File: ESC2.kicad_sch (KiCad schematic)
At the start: 35 parts, among them J10 MOTOR1, J9 SWD1, Q4 XRS306D, Q5 XRS306D, Q6 XRS306D, U10 STM32G071GBUxN, U11 DRV8300D

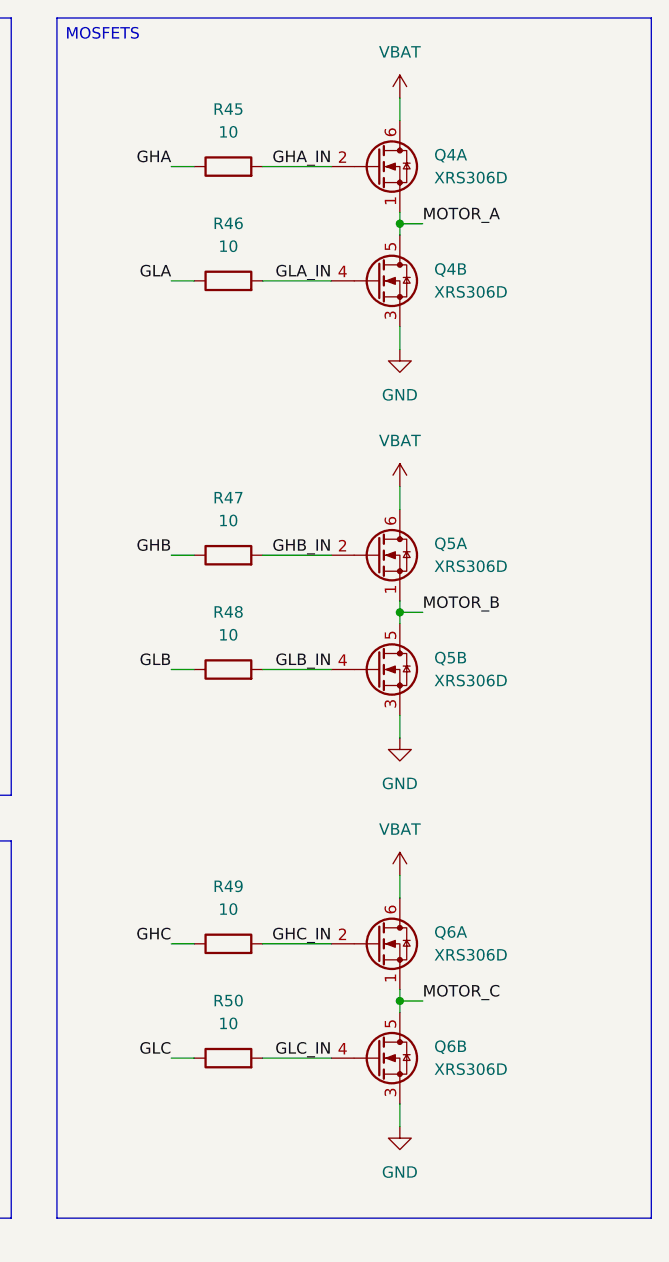
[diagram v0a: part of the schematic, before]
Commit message: License and ESC layout
Added a file extension to the license.
Updated the second ESC layout.

TODO:
Continue the ESC layout.
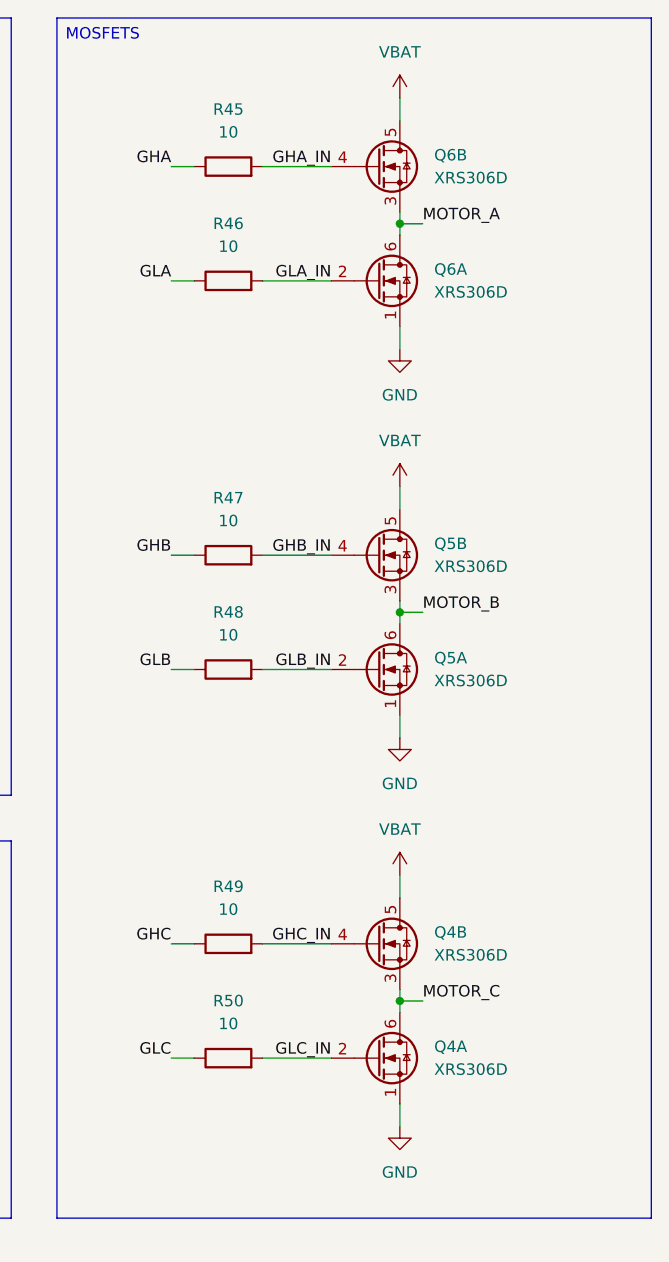
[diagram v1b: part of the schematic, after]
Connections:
- net GHA_IN: now also Q6.4 (G); no longer Q4.2 (G)
- net GHB_IN: now also Q5.4 (G); no longer Q5.2 (G)
- net GHC_IN: now also Q4.4 (G); no longer Q6.2 (G)
- net GLA_IN: now also Q6.2 (G); no longer Q4.4 (G)
- net GLB_IN: now also Q5.2 (G); no longer Q5.4 (G)
- net GLC_IN: now also Q4.2 (G); no longer Q6.4 (G)
- net GND: now also Q4.1 (S), Q5.1 (S), Q6.1 (S); no longer Q4.3 (S), Q5.3 (S), Q6.3 (S)
- net MOTOR_A: now also Q6.3 (S), Q6.6 (D); no longer Q4.1 (S), Q4.5 (D)
- net MOTOR_B: now also Q5.3 (S), Q5.6 (D); no longer Q5.1 (S), Q5.5 (D)
- net MOTOR_C: now also Q4.3 (S), Q4.6 (D); no longer Q6.1 (S), Q6.5 (D)
- net VBAT: now also Q4.5 (D), Q5.5 (D), Q6.5 (D); no longer Q4.6 (D), Q5.6 (D), Q6.6 (D)
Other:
- moved on the sheet: Q4A, Q4B, Q5A, Q5B, Q6A, Q6B

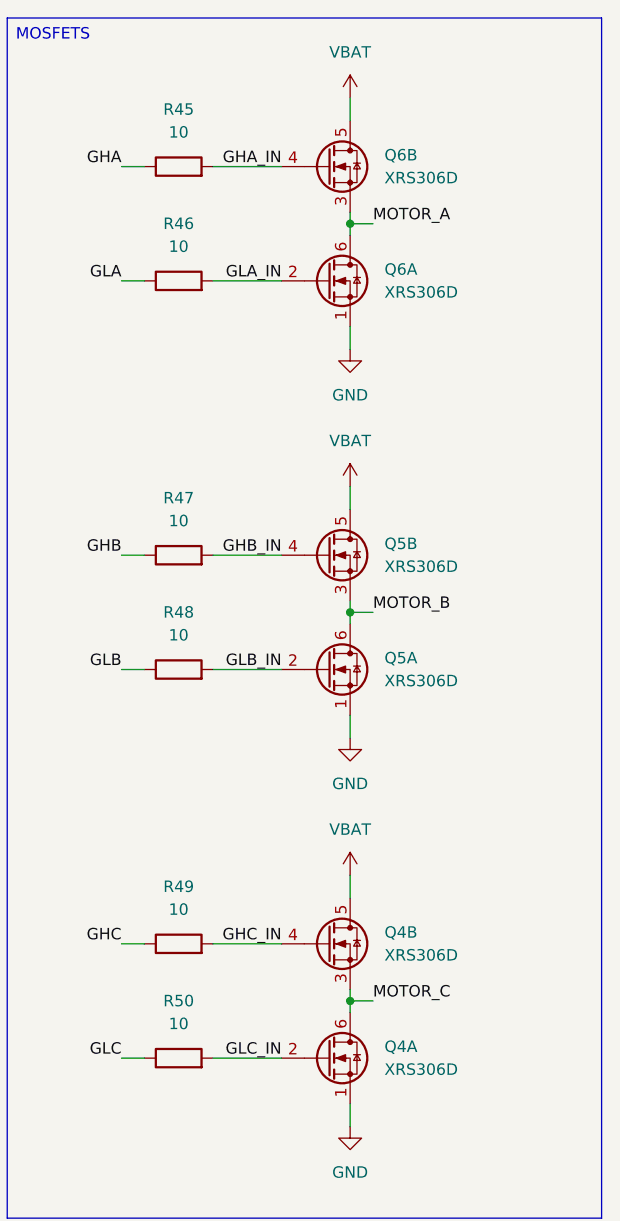
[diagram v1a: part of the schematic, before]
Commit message: MCU layout
Updated the schematic labels.
Continued the MCU layout.
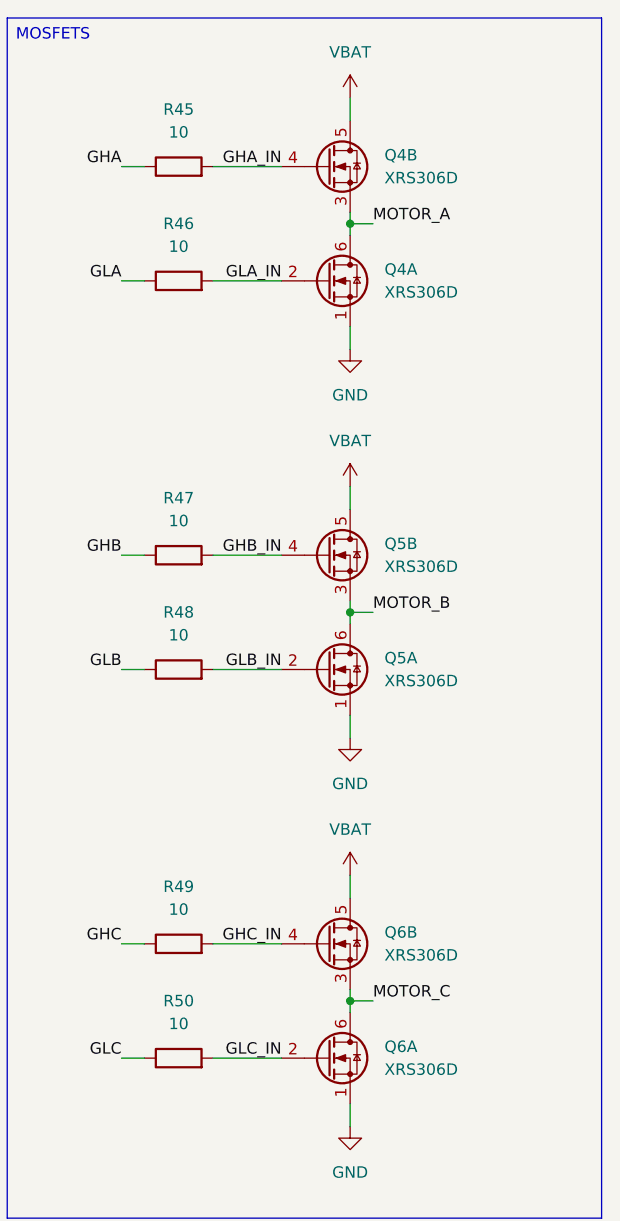
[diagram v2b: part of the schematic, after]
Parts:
- renumbered Q6 to Q4, Q4 to Q6
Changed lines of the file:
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@@
 		(dnp no)
 		(fields_autoplaced yes)
-		(property "Reference" "Q4"
+		(property "Reference" "Q6"
 			(at 250.19 124.4599 0)
 			(effects
@@
 			(project "ThunderHorse"
 				(path "/ac187c6c-fa53-41cc-bce1-6f39a42a92e8/807a5f6f-4255-4cf0-8d90-acd62bb18590/5c810e84-f116-497a-8ed3-5f68f4ce3b3e"
-					(reference "Q4")
+					(reference "Q6")
 					(unit 2)
 				)
@@
 		(dnp no)
 		(fields_autoplaced yes)
-		(property "Reference" "Q6"
+		(property "Reference" "Q4"
 			(at 250.19 38.0999 0)
 			(effects
@@
 			(project "ThunderHorse"
 				(path "/ac187c6c-fa53-41cc-bce1-6f39a42a92e8/807a5f6f-4255-4cf0-8d90-acd62bb18590/5c810e84-f116-497a-8ed3-5f68f4ce3b3e"
-					(reference "Q6")
+					(reference "Q4")
 					(unit 2)
 				)
@@
 		(dnp no)
 		(fields_autoplaced yes)
-		(property "Reference" "Q6"
+		(property "Reference" "Q4"
 			(at 250.19 50.7999 0)
 			(effects
@@
 			(project "ThunderHorse"
 				(path "/ac187c6c-fa53-41cc-bce1-6f39a42a92e8/807a5f6f-4255-4cf0-8d90-acd62bb18590/5c810e84-f116-497a-8ed3-5f68f4ce3b3e"
-					(reference "Q6")
+					(reference "Q4")
 					(unit 1)
 				)
@@
 		(dnp no)
 		(fields_autoplaced yes)
-		(property "Reference" "Q4"
+		(property "Reference" "Q6"
 			(at 250.19 137.1599 0)
 			(effects
@@
 			(project "ThunderHorse"
 				(path "/ac187c6c-fa53-41cc-bce1-6f39a42a92e8/807a5f6f-4255-4cf0-8d90-acd62bb18590/5c810e84-f116-497a-8ed3-5f68f4ce3b3e"
-					(reference "Q4")
-					(unit 1)
-				)
+					(reference "Q6")
+					(unit 1)
+				)

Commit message: Schematic revision
Added an ESP32 C3 for the ELRS receiver.
Updated the protection approach for the board.
Updated the net nodes.
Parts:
- removed C53, C54, C55: 10u, Capacitor_SMD:C_1206_3216Metric, symbol Device:C
- added C48, C50: 22u, Capacitor_SMD:C_1206_3216Metric, symbol Device:C
- C49, C51, C52: value 10u -> 22u
- renumbered C48 to C46, C50 to C47, C56 to C53, C57 to C54, C58 to C55, C59 to C56, Q4 to Q5, Q5 to Q6, Q6 to Q7, R35 to R33, R36 to R34, R37 to R35, R38 to R36, R39 to R37, R40 to R38, R41 to R39, R42 to R40, R43 to R41, R44 to R42, R45 to R43, R46 to R44, R47 to R45, R48 to R46, R49 to R47, R50 to R48, U11 to U10, U10 to U9
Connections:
- net GND: now also C48.2, C50.2
- net VBAT: now also C48.1, C50.1

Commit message: IMU filtering and layout
Added a missing capacitor for the IMU.
Updated the PCB layout.
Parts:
- renumbered C46 to C41, C47 to C42, C48 to C43, C49 to C44, C50 to C45, C51 to C46, C52 to C47, C53 to C48, C54 to C49, C55 to C50, C56 to C51

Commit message: Oscillator and IMU layout
Updated the oscillator layout for the RP2350.
Updated the IMU layout for the IMU.
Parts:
- renumbered C41 to C42, C42 to C43, C43 to C44, C44 to C45, C45 to C46, C46 to C47, C47 to C48, C48 to C49, C49 to C50, C50 to C51, C51 to C52
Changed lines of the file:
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@@
 		(dnp no)
 		(fields_autoplaced yes)
-		(property "Reference" "C44"
+		(property "Reference" "C45"
 			(at 59.69 175.2599 0)
 			(effects
@@
 			(project "ThunderHorse"
 				(path "/ac187c6c-fa53-41cc-bce1-6f39a42a92e8/807a5f6f-4255-4cf0-8d90-acd62bb18590/5c810e84-f116-497a-8ed3-5f68f4ce3b3e"
-					(reference "C44")
+					(reference "C45")
 					(unit 1)
 				)
@@
 		(dnp no)
 		(fields_autoplaced yes)
-		(property "Reference" "C47"
+		(property "Reference" "C48"
 			(at 97.79 175.2599 0)
 			(effects
@@
 			(project "ThunderHorse"
 				(path "/ac187c6c-fa53-41cc-bce1-6f39a42a92e8/807a5f6f-4255-4cf0-8d90-acd62bb18590/5c810e84-f116-497a-8ed3-5f68f4ce3b3e"
-					(reference "C47")
+					(reference "C48")
 					(unit 1)
 				)
@@
 		(dnp no)
 		(fields_autoplaced yes)
-		(property "Reference" "C41"
+		(property "Reference" "C42"
 			(at 34.29 44.4499 0)
 			(effects
@@
 			(project "ThunderHorse"
 				(path "/ac187c6c-fa53-41cc-bce1-6f39a42a92e8/807a5f6f-4255-4cf0-8d90-acd62bb18590/5c810e84-f116-497a-8ed3-5f68f4ce3b3e"
-					(reference "C41")
+					(reference "C42")
 					(unit 1)
 				)
@@
 		(dnp no)
 		(fields_autoplaced yes)
-		(property "Reference" "C50"
+		(property "Reference" "C51"
 			(at 184.15 58.42 90)
 			(effects
@@
 			(project "ThunderHorse"
 				(path "/ac187c6c-fa53-41cc-bce1-6f39a42a92e8/807a5f6f-4255-4cf0-8d90-acd62bb18590/5c810e84-f116-497a-8ed3-5f68f4ce3b3e"
-					(reference "C50")
+					(reference "C51")
 					(unit 1)
 				)
@@
 		(dnp no)
 		(fields_autoplaced yes)
-		(property "Reference" "C51"
+		(property "Reference" "C52"
 			(at 184.15 72.39 90)
 			(effects
@@
 			(project "ThunderHorse"
 				(path "/ac187c6c-fa53-41cc-bce1-6f39a42a92e8/807a5f6f-4255-4cf0-8d90-acd62bb18590/5c810e84-f116-497a-8ed3-5f68f4ce3b3e"
-					(reference "C51")
+					(reference "C52")
 					(unit 1)
 				)
@@
 		(dnp no)
 		(fields_autoplaced yes)
-		(property "Reference" "C45"
+		(property "Reference" "C46"
 			(at 72.39 175.2599 0)
 			(effects
@@
 			(project "ThunderHorse"
 				(path "/ac187c6c-fa53-41cc-bce1-6f39a42a92e8/807a5f6f-4255-4cf0-8d90-acd62bb18590/5c810e84-f116-497a-8ed3-5f68f4ce3b3e"
-					(reference "C45")
+					(reference "C46")
 					(unit 1)
 				)
@@
 		(on_board yes)
 		(dnp no)
-		(property "Reference" "C43"
+		(property "Reference" "C44"
 			(at 46.99 175.2599 0)
 			(effects
@@
 			(project "ThunderHorse"
 				(path "/ac187c6c-fa53-41cc-bce1-6f39a42a92e8/807a5f6f-4255-4cf0-8d90-acd62bb18590/5c810e84-f116-497a-8ed3-5f68f4ce3b3e"
-					(reference "C43")
+					(reference "C44")
 					(unit 1)
 				)
@@
 		(dnp no)
 		(fields_autoplaced yes)
-		(property "Reference" "C49"
+		(property "Reference" "C50"
 			(at 184.15 44.45 90)
 			(effects
@@
 			(project "ThunderHorse"
 				(path "/ac187c6c-fa53-41cc-bce1-6f39a42a92e8/807a5f6f-4255-4cf0-8d90-acd62bb18590/5c810e84-f116-497a-8ed3-5f68f4ce3b3e"
-					(reference "C49")
+					(reference "C50")
 					(unit 1)
 				)
@@
 		(dnp no)
 		(fields_autoplaced yes)
-		(property "Reference" "C46"
+		(property "Reference" "C47"
 			(at 85.09 175.2599 0)
 			(effects
@@
 			(project "ThunderHorse"
 				(path "/ac187c6c-fa53-41cc-bce1-6f39a42a92e8/807a5f6f-4255-4cf0-8d90-acd62bb18590/5c810e84-f116-497a-8ed3-5f68f4ce3b3e"
-					(reference "C46")
+					(reference "C47")
 					(unit 1)
 				)
@@
 		(dnp no)
 		(fields_autoplaced yes)
-		(property "Reference" "C48"
+		(property "Reference" "C49"
 			(at 144.78 40.6399 0)
 			(effects
@@
 			(project "ThunderHorse"
 				(path "/ac187c6c-fa53-41cc-bce1-6f39a42a92e8/807a5f6f-4255-4cf0-8d90-acd62bb18590/5c810e84-f116-497a-8ed3-5f68f4ce3b3e"
-					(reference "C48")
+					(reference "C49")
 					(unit 1)
 				)
@@
 		(dnp no)
 		(fields_autoplaced yes)
-		(property "Reference" "C42"
+		(property "Reference" "C43"
 			(at 45.72 44.4499 0)
 			(effects
@@
 			(project "ThunderHorse"
 				(path "/ac187c6c-fa53-41cc-bce1-6f39a42a92e8/807a5f6f-4255-4cf0-8d90-acd62bb18590/5c810e84-f116-497a-8ed3-5f68f4ce3b3e"
-					(reference "C42")
+					(reference "C43")
 					(unit 1)
 				)

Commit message: Power and ESC layout
Updated the power layout.
Updated the ESC layout.

TODO:
Improve track spacing for the ESC.
Complete the power connections.
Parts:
- C49: footprint Capacitor_SMD:C_0805_2012Metric -> Capacitor_SMD:C_0603_1608Metric
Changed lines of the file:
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@@
 			)
 		)
-		(property "Footprint" "Capacitor_SMD:C_0805_2012Metric"
+		(property "Footprint" "Capacitor_SMD:C_0603_1608Metric"
 			(at 141.9352 45.72 0)
 			(effects

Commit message: Voltage detection
Added a VBUS voltage detection for the RP.
Minor layout changes.
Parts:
- renumbered C49 to C42, C42 to C43, C43 to C44, C50 to C45, C51 to C46, C52 to C47, C44 to C48, C45 to C49, C46 to C50, C47 to C51, C48 to C52, R43 to R35, R44 to R36, R45 to R38, R46 to R39, R47 to R40, R34 to R41, R38 to R42, R41 to R43, R33 to R44, R36 to R45, R40 to R46, R48 to R47, R35 to R48, R39 to R49, R42 to R50
